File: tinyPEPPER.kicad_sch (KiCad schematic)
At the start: 7 parts

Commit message: added further parts
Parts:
- added TP? (x2): TP, custom:TP_powerpad, symbol custom:TP
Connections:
- new net FC/RC_RX: TP?.1
- new net FC/RC_TX: TP?.1
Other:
- sheet MCU renamed FC
- sheet POWER1 renamed POWER
- sheet FC ports: added GND, GPS_RX, GPS_TX, RC_RX, RC_TX, TELEM_RX, TELEM_TX; removed none
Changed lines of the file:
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@@
   (junction (at 162.56 34.29) (diameter 0) (color 0 0 0 0)
   )
+  (junction (at 59.69 71.12) (diameter 0) (color 0 0 0 0)
+  )
   (junction (at 125.73 34.29) (diameter 0) (color 0 0 0 0)
   )
-  (wire (pts (xy 57.15 71.12) (xy 151.13 71.12))
+  (wire (pts (xy 57.15 71.12) (xy 59.69 71.12))
     (stroke (width 0) (type default) (color 0 0 0 0))
   )
@@
     (stroke (width 0) (type default) (color 0 0 0 0))
   )
+  (wire (pts (xy 63.5 91.44) (xy 59.69 91.44))
+    (stroke (width 0) (type default) (color 0 0 0 0))
+  )
   (wire (pts (xy 166.37 59.69) (xy 168.91 59.69))
     (stroke (width 0) (type default) (color 0 0 0 0))
@@
     (stroke (width 0) (type default) (color 0 0 0 0))
   )
-  (wire (pts (xy 146.05 95.25) (xy 128.27 95.25))
+  (wire (pts (xy 146.05 95.25) (xy 129.54 95.25))
     (stroke (width 0) (type default) (color 0 0 0 0))
   )
@@
     (stroke (width 0) (type default) (color 0 0 0 0))
   )
+  (wire (pts (xy 50.8 114.3) (xy 63.5 114.3))
+    (stroke (width 0) (type default) (color 0 0 0 0))
+  )
   (wire (pts (xy 168.91 43.18) (xy 154.94 43.18))
     (stroke (width 0) (type default) (color 0 0 0 0))
@@
     (stroke (width 0) (type default) (color 0 0 0 0))
   )
+  (wire (pts (xy 50.8 118.11) (xy 63.5 118.11))
+    (stroke (width 0) (type default) (color 0 0 0 0))
+  )
   (wire (pts (xy 168.91 130.81) (xy 138.43 130.81))
     (stroke (width 0) (type default) (color 0 0 0 0))
@@
     (stroke (width 0) (type default) (color 0 0 0 0))
   )
-  (wire (pts (xy 138.43 99.06) (xy 128.27 99.06))
+  (wire (pts (xy 138.43 99.06) (xy 129.54 99.06))
     (stroke (width 0) (type default) (color 0 0 0 0))
   )
@@
     (stroke (width 0) (type default) (color 0 0 0 0))
   )
-  (wire (pts (xy 157.48 91.44) (xy 128.27 91.44))
+  (wire (pts (xy 157.48 91.44) (xy 129.54 91.44))
     (stroke (width 0) (type default) (color 0 0 0 0))
   )
@@
     (stroke (width 0) (type default) (color 0 0 0 0))
   )
-  (wire (pts (xy 154.94 87.63) (xy 128.27 87.63))
+  (wire (pts (xy 154.94 87.63) (xy 129.54 87.63))
     (stroke (width 0) (type default) (color 0 0 0 0))
   )
@@
     (stroke (width 0) (type default) (color 0 0 0 0))
   )
+  (wire (pts (xy 59.69 71.12) (xy 151.13 71.12))
+    (stroke (width 0) (type default) (color 0 0 0 0))
+  )
   (wire (pts (xy 168.91 101.6) (xy 146.05 101.6))
     (stroke (width 0) (type default) (color 0 0 0 0))
@@
   )
   (wire (pts (xy 157.48 73.66) (xy 157.48 91.44))
+    (stroke (width 0) (type default) (color 0 0 0 0))
+  )
+  (wire (pts (xy 59.69 91.44) (xy 59.69 71.12))
     (stroke (width 0) (type default) (color 0 0 0 0))
   )
@@
   (label "VBAT" (at 100.33 27.94 0)
     (effects (font (size 1.524 1.524)) (justify left bottom))
-  )
-  (hierarchical_label "GND" (shape input) (at 69.85 45.72 180)
-    (effects (font (size 1.524 1.524)) (justify right))
   )
   (symbol (lib_id "custom:TP") (at 92.71 27.94 180) (unit 1)
@@
       (effects (font (size 1.524 1.524)))
     )
+  )
+  (symbol (lib_id "custom:TP") (at 43.18 114.3 180) (unit 1)
+    (in_bom yes) (on_board yes)
+    (property "Reference" "TP?" (id 0) (at 39.37 114.3 0)
+      (effects (font (size 1.524 1.524)))
+    )
+    (property "Value" "TP" (id 1) (at 39.37 118.11 0)
+      (effects (font (size 1.524 1.524)) hide)
+    )
+    (property "Footprint" "custom:TP_powerpad" (id 2) (at 43.18 114.3 0)
+      (effects (font (size 1.524 1.524)) hide)
+    )
+    (property "Datasheet" "~" (id 3) (at 43.18 114.3 0)
+      (effects (font (size 1.524 1.524)))
+    )
+    (pin "1")
+  )
+  (symbol (lib_id "custom:TP") (at 43.18 118.11 180) (unit 1)
+    (in_bom yes) (on_board yes)
+    (property "Reference" "TP?" (id 0) (at 39.37 118.11 0)
+      (effects (font (size 1.524 1.524)))
+    )
+    (property "Value" "TP" (id 1) (at 39.37 121.92 0)
+      (effects (font (size 1.524 1.524)) hide)
+    )
+    (property "Footprint" "custom:TP_powerpad" (id 2) (at 43.18 118.11 0)
+      (effects (font (size 1.524 1.524)) hide)
+    )
+    (property "Datasheet" "~" (id 3) (at 43.18 118.11 0)
+      (effects (font (size 1.524 1.524)))
+    )
+    (pin "1")
   )
   (sheet (at 168.91 25.4) (size 48.26 21.59) (fields_autoplaced)
@@
     (stroke (width 0.1524) (type solid) (color 0 0 0 0))
     (fill (color 0 0 0 0.0000))
-    (property "Sheet name" "POWER1" (id 0) (at 22.86 58.9784 0)
+    (property "Sheet name" "POWER" (id 0) (at 22.86 58.9784 0)
       (effects (font (size 1.27 1.27)) (justify left bottom))
     )
@@
     )
   )
-  (sheet (at 63.5 81.28) (size 64.77 39.37) (fields_autoplaced)
+  (sheet (at 63.5 81.28) (size 66.04 76.2) (fields_autoplaced)
     (stroke (width 0.1524) (type solid) (color 0 0 0 0))
     (fill (color 0 0 0 0.0000))
-    (property "Sheet name" "MCU" (id 0) (at 63.5 80.5684 0)
+    (property "Sheet name" "FC" (id 0) (at 63.5 80.5684 0)
       (effects (font (size 1.27 1.27)) (justify left bottom))
     )
-    (property "Sheet file" "mcu.kicad_sch" (id 1) (at 63.5 121.2346 0)
+    (property "Sheet file" "mcu.kicad_sch" (id 1) (at 63.5 158.0646 0)
       (effects (font (size 1.27 1.27)) (justify left top))
     )
@@
       (effects (font (size 1.27 1.27)) (justify left))
     )
-    (pin "MOTOR 4" output (at 128.27 99.06 0)
+    (pin "MOTOR 4" output (at 129.54 99.06 0)
       (effects (font (size 1.27 1.27)) (justify right))
     )
-    (pin "MOTOR 2" output (at 128.27 91.44 0)
+    (pin "MOTOR 2" output (at 129.54 91.44 0)
       (effects (font (size 1.27 1.27)) (justify right))
     )
-    (pin "MOTOR 3" output (at 128.27 95.25 0)
+    (pin "MOTOR 3" output (at 129.54 95.25 0)
       (effects (font (size 1.27 1.27)) (justify right))
     )
-    (pin "MOTOR 1" output (at 128.27 87.63 0)
+    (pin "MOTOR 1" output (at 129.54 87.63 0)
       (effects (font (size 1.27 1.27)) (justify right))
+    )
+    (pin "RC_TX" output (at 63.5 114.3 180)
+      (effects (font (size 1.27 1.27)) (justify left))
+    )
+    (pin "RC_RX" input (at 63.5 118.11 180)
+      (effects (font (size 1.27 1.27)) (justify left))
+    )
+    (pin "TELEM_TX" output (at 63.5 125.73 180)
+      (effects (font (size 1.27 1.27)) (justify left))
+    )
+    (pin "TELEM_RX" input (at 63.5 129.54 180)
+      (effects (font (size 1.27 1.27)) (justify left))
+    )
+    (pin "GPS_TX" output (at 63.5 137.16 180)
+      (effects (font (size 1.27 1.27)) (justify left))
+    )
+    (pin "GPS_RX" input (at 63.5 140.97 180)
+      (effects (font (size 1.27 1.27)) (justify left))
+    )
+    (pin "GND" input (at 63.5 91.44 180)
+      (effects (font (size 1.27 1.27)) (justify left))
     )
   )
@@
       (reference "H4") (unit 1) (value "hole") (footprint "custom:mouting_hole")
     )
+    (path "/548f1ca0-1bbc-4fe3-9d3c-05bf73366ef9/bb8dd361-f36d-4a8f-aaab-17e3bc43efc5"
+      (reference "J?") (unit 1) (value "Micro_SD_Card") (footprint "")
+    )
     (path "/00000000-0000-0000-0000-000057f7ac44/00000000-0000-0000-0000-000057f78eab"
       (reference "OUT_A201") (unit 1) (value "TP") (footprint "custom:TP_PHASE_SMD")
@@
       (reference "OUT_C501") (unit 1) (value "TP") (footprint "custom:TP_PHASE_SMD")
     )
+    (path "/548f1ca0-1bbc-4fe3-9d3c-05bf73366ef9/ddea7687-3cfe-4386-943f-a553ad180ea7"
+      (reference "P?") (unit 1) (value "USB_C_Plug") (footprint "")
+    )
     (path "/00000000-0000-0000-0000-000057f7ac44/00000000-0000-0000-0000-000057f79dfa"
       (reference "R201") (unit 1) (value "1k") (footprint "custom:R_0402_CUSTOM")
@@
       (reference "TP502") (unit 1) (value "TP") (footprint "custom:TP_smd_0.5x0.8")
     )
+    (path "/62b50e1f-03ce-46d0-9d6c-4a43fd1697bd"
+      (reference "TP?") (unit 1) (value "TP") (footprint "custom:TP_powerpad")
+    )
+    (path "/f627b886-8a26-4e3a-b337-f6ec0456b8a0"
+      (reference "TP?") (unit 1) (value "TP") (footprint "custom:TP_powerpad")
+    )
     (path "/00000000-0000-0000-0000-000057f7ac44/00000000-0000-0000-0000-000057f76060"
       (reference "U201") (unit 1) (value "EFM8BB21") (footprint "custom:QFN20")
@@
       (reference "U501") (unit 1) (value "EFM8BB21") (footprint "custom:QFN20")
     )
+    (path "/548f1ca0-1bbc-4fe3-9d3c-05bf73366ef9/58b9ced7-8dfd-4f1f-8b66-b2f1b799f8ac"
+      (reference "U?") (unit 1) (value "ICM-20602") (footprint "Package_LGA:LGA-16_3x3mm_P0.5mm_LayoutBorder3x5y")
+    )
+    (path "/548f1ca0-1bbc-4fe3-9d3c-05bf73366ef9/70a189b0-e838-46a3-b802-0a715752df29"
+      (reference "U?") (unit 1) (value "BMP280") (footprint "Package_LGA:Bosch_LGA-8_2x2.5mm_P0.65mm_ClockwisePinNumbering")
+    )
     (path "/548f1ca0-1bbc-4fe3-9d3c-05bf73366ef9/82b04b62-a3fa-4e38-ab66-3bbb25081990"
       (reference "U?") (unit 1) (value "STM32F405RGTx") (footprint "Package_QFP:LQFP-64_10x10mm_P0.5mm")
     )
-  )
+    (path "/3fc6e526-3a3c-4a34-8308-04e953347e49/cf6d4553-2f2e-4fbd-be7f-493fbe879623"
+      (reference "U?") (unit 1) (value "TPS54202DDC") (footprint "Package_TO_SOT_SMD:SOT-23-6")
+    )
+  )

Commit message: added 3v3-reg
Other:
- sheet POWER ports: added VBUS; removed none
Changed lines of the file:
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@@
+      (effects (font (size 1.27 1.27)) (justify right))
+    )
+    (pin "VBUS" input (at 38.1 59.69 90)
       (effects (font (size 1.27 1.27)) (justify right))
     )
@@
       (reference "C1000") (unit 1) (value "47u") (footprint "Capacitors_SMD:C_0805")
     )
+    (path "/3fc6e526-3a3c-4a34-8308-04e953347e49/158f45f9-10b1-4a6d-8f87-5e4fadc7cc75"
+      (reference "C?") (unit 1) (value "1uF") (footprint "")
+    )
     (path "/3fc6e526-3a3c-4a34-8308-04e953347e49/3bf447e6-b838-443f-ba7b-0ff0a7f2c52e"
       (reference "C?") (unit 1) (value "10uF") (footprint "")
@@
       (reference "C?") (unit 1) (value "22uF") (footprint "")
     )
+    (path "/3fc6e526-3a3c-4a34-8308-04e953347e49/b6c2e52c-1c61-4c1c-a0f9-5b4019ce944a"
+      (reference "C?") (unit 1) (value "1uF") (footprint "")
+    )
+    (path "/3fc6e526-3a3c-4a34-8308-04e953347e49/8bc6cc23-bdd7-465d-9397-4a89e0758342"
+      (reference "D?") (unit 1) (value "DIODE") (footprint "")
+    )
     (path "/00000000-0000-0000-0000-000057f7ac44/00000000-0000-0000-0000-000057f76a91"
       (reference "FET201") (unit 1) (value "IRLML6244") (footprint "TO_SOT_Packages_SMD:SOT-23")
@@
       (reference "U501") (unit 1) (value "EFM8BB21") (footprint "custom:QFN20")
     )
+    (path "/3fc6e526-3a3c-4a34-8308-04e953347e49/0895fa58-747e-4da1-ad23-c6fbae36577f"
+      (reference "U?") (unit 1) (value "RT9013-33GB") (footprint "SOT94P279X129-5N")
+    )
     (path "/548f1ca0-1bbc-4fe3-9d3c-05bf73366ef9/58b9ced7-8dfd-4f1f-8b66-b2f1b799f8ac"

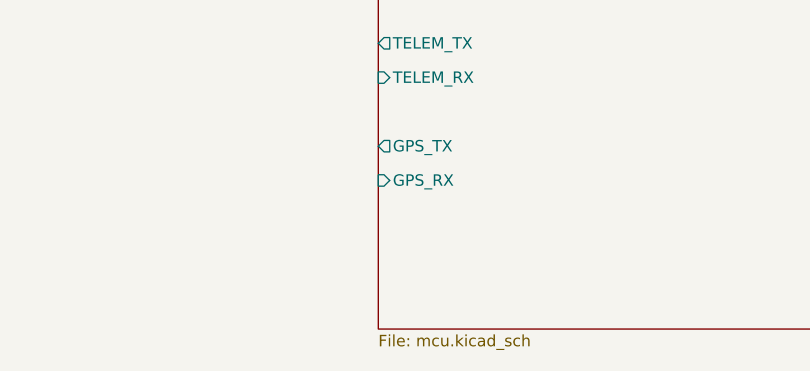
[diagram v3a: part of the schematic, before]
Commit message: added correct usb plug
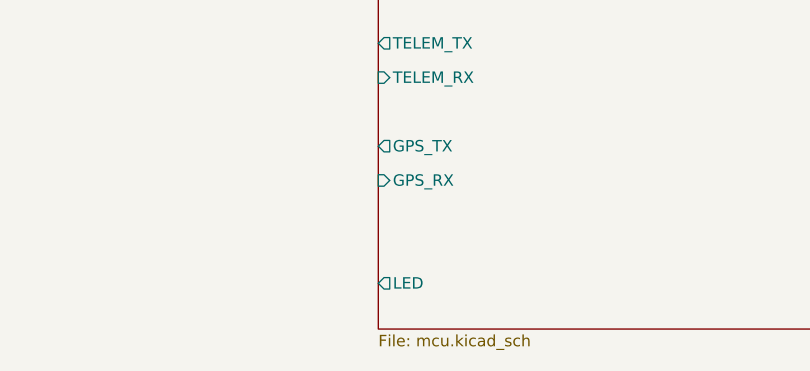
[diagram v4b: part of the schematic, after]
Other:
- sheet FC ports: added LED; removed none
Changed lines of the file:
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@@
+      (effects (font (size 1.27 1.27)) (justify left))
+    )
+    (pin "LED" output (at 63.5 152.4 180)
       (effects (font (size 1.27 1.27)) (justify left))
     )
@@
       (reference "H4") (unit 1) (value "hole") (footprint "custom:mouting_hole")
     )
+    (path "/548f1ca0-1bbc-4fe3-9d3c-05bf73366ef9/738e864b-2adb-4de5-94f2-72e9cbe7ffe9"
+      (reference "J?") (unit 1) (value "TYPE-C-31-M-12") (footprint "HRO_TYPE-C-31-M-12")
+    )
     (path "/548f1ca0-1bbc-4fe3-9d3c-05bf73366ef9/bb8dd361-f36d-4a8f-aaab-17e3bc43efc5"
       (reference "J?") (unit 1) (value "Micro_SD_Card") (footprint "")
@@
       (reference "OUT_C501") (unit 1) (value "TP") (footprint "custom:TP_PHASE_SMD")
     )
-    (path "/548f1ca0-1bbc-4fe3-9d3c-05bf73366ef9/ddea7687-3cfe-4386-943f-a553ad180ea7"
-      (reference "P?") (unit 1) (value "USB_C_Plug") (footprint "")
-    )
     (path "/00000000-0000-0000-0000-000057f7ac44/00000000-0000-0000-0000-000057f79dfa"
